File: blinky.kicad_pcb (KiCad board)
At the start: 2 copper layers, 69.9 x 70 mm, 58 parts, among them J1 MIC_CLK, J10 DEBUG, J11 SWD, J12 BATTERY, J13 UART, J14 5V, J15 3V3, J2 MIC_DOUT, J3 LED_DIN, J4 ACCEL_MISO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

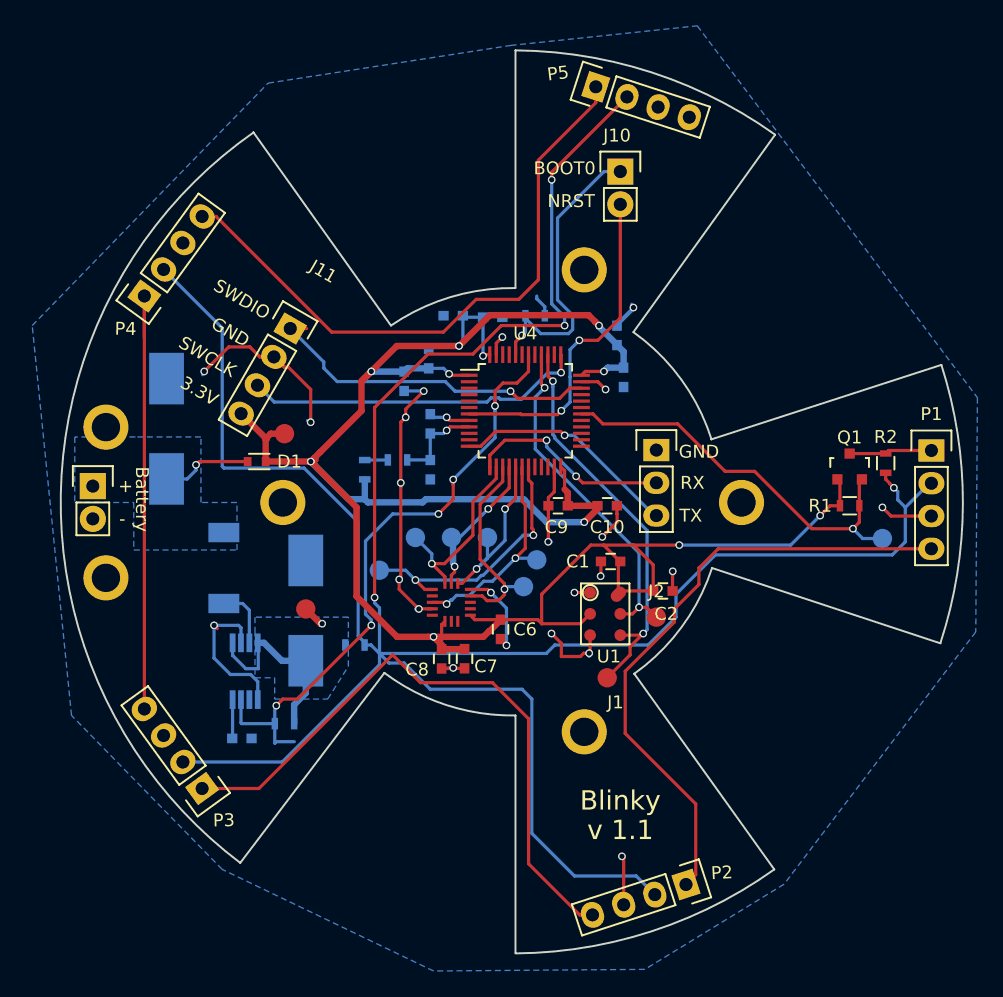
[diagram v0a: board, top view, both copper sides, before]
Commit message: Add heartbeat led
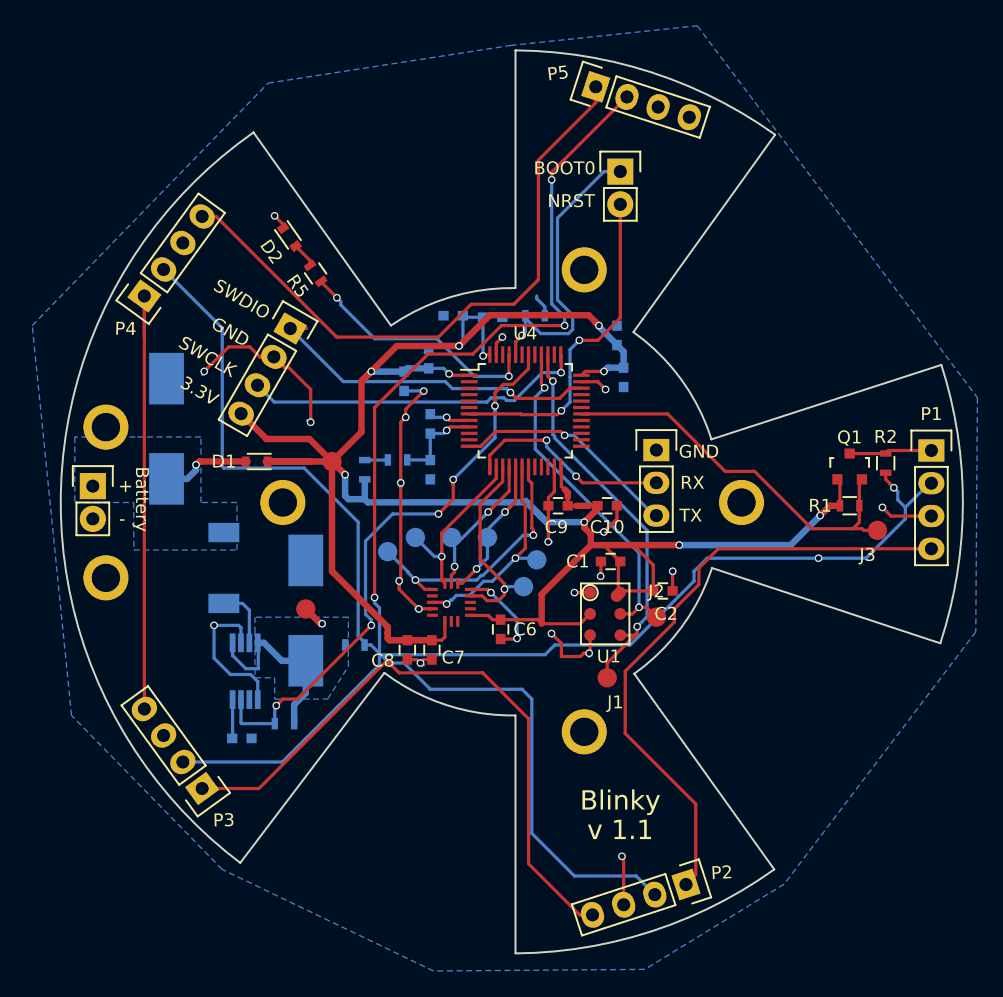
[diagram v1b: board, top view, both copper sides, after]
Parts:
- added D2: LED, Diodes_SMD:D_0603, F.Cu at (114.8, 53.1)
- added R5: 0, Resistors_SMD:R_0603, F.Cu at (116.8, 55.9)
- D1: value D_Schottky_0.5A_20V -> D_Schottky_0.1A_30V; footprint Diodes_SMD:SOD-523 -> Diodes_SMD:D_0603
- J3: moved to F.Cu
- moved J15 4.27 mm to (118.1, 70.5)
- moved C8 2.75 mm to (124.0, 85.1)
- moved C7 2.62 mm to (125.9, 85.1)
- moved J9 1.58 mm to (122.4, 77.5)
- moved J3 0.74 mm to (160.4, 75.8)
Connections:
- U4 pad 45: /MCU/PB8 -> /LED_HB
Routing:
- net /LED_HB: track 0.00 -> 19.5 mm, vias 0 -> 2
- net /POWER_LBO: track 48.5 -> 45.2 mm
- net GND: track 95.8 -> 92.9 mm
- net Net-(D2-Pad2): track 0.00 -> 1.97 mm
- net /ACCEL_MISO: track 13.2 -> 11.5 mm
- net Net-(P1-Pad2): track 206.9 -> 205.3 mm, vias 4 -> 5
- net /ACCEL_CS: track 14.7 -> 13.5 mm
- net +3V3: track 182.6 -> 181.9 mm, vias 11 -> 10
- net /LED_DATAIN: track 31.4 -> 30.8 mm, vias 1 -> 0
- net /MIC_CLK: track 31.3 -> 30.8 mm
- net Net-(P2-Pad4): track 49.5 -> 49.0 mm

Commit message: Add shortcut to enable 3V3 Only mode
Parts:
- added R8: 0, Resistors_SMD:R_0805, F.Cu at (118.1, 81.0)
- moved J14 3.42 mm to (112.8, 81.0)
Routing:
- net GND: track 92.9 -> 116.5 mm, vias 24 -> 28
- net +5V: track 18.3 -> 20.4 mm, vias 1 -> 2
- net +3V3: track 181.9 -> 180.7 mm

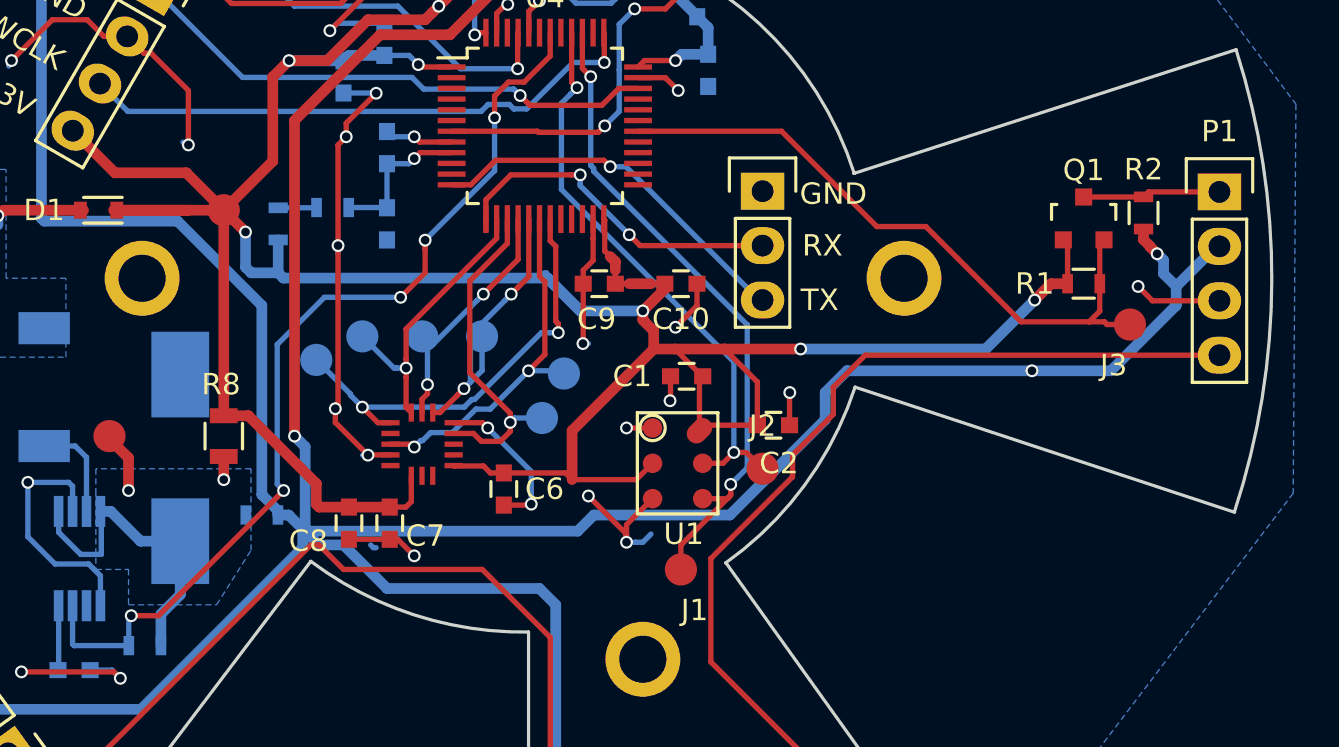
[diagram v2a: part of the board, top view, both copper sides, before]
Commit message: change level shifter
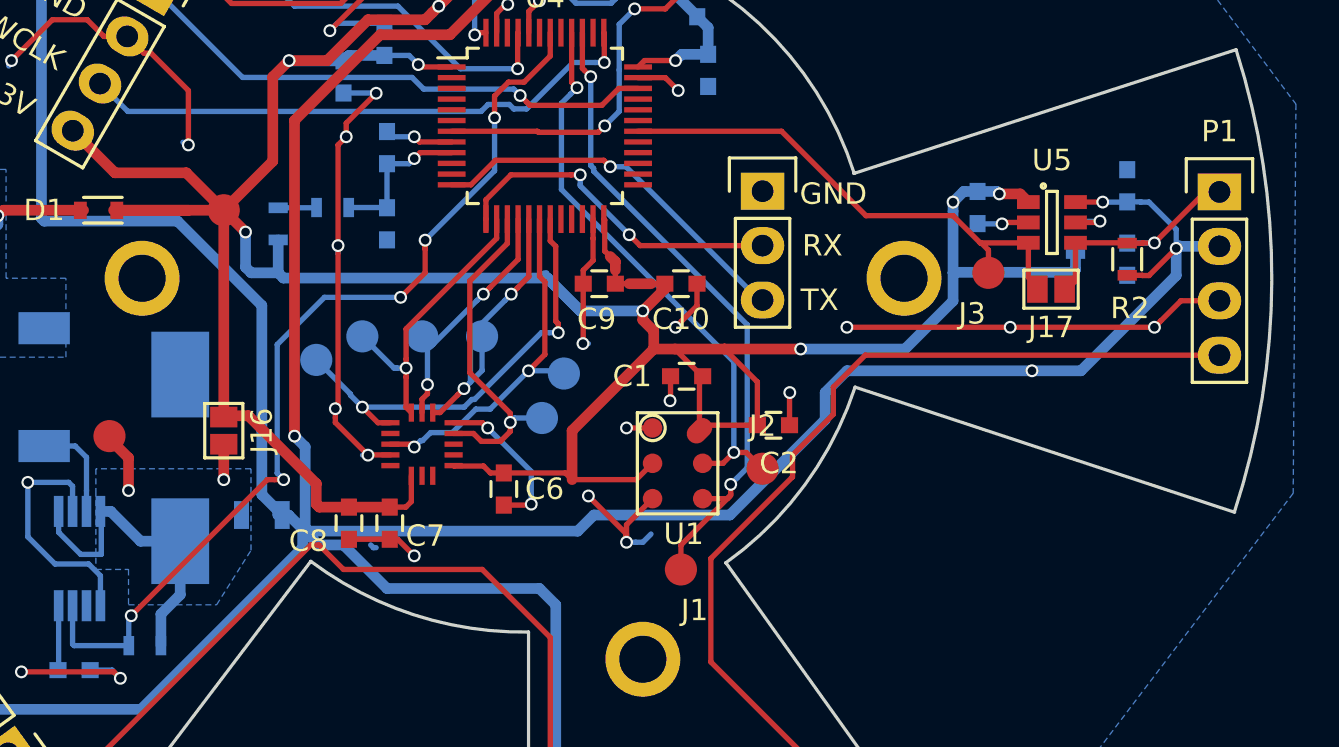
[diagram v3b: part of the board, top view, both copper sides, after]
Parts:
- removed Q1: BSS138, TO_SOT_Packages_SMD:SOT-23
- removed R8: 0, Resistors_SMD:R_0805
- added C19: 100nF, Capacitors_SMD:C_0603, B.Cu at (153.3, 70.4)
- added C20: NA, Capacitors_SMD:C_0603, B.Cu at (160.3, 69.3)
- added C21: NA, Capacitors_SMD:C_0603, B.Cu at (160.3, 72.8)
- added J16: GS2, Connectors:GS2, F.Cu at (118.1, 80.8)
- added J17: GS2, Connectors:GS2, F.Cu at (156.7, 74.2)
- added U5: TXS0101, TO_SOT_Packages_SMD:SOT-23-6, F.Cu at (156.8, 71.1)
- R1: value 10k -> NA; moved to B.Cu
- R2: value 10k -> NA
- R4: footprint Resistors_SMD:R_0603 -> Resistors_SMD:R_0805
- moved J3 7.03 mm to (153.8, 73.4)
- moved R2 2.29 mm to (160.3, 72.8)
- moved R1 2.19 mm to (157.9, 71.8), turned to 90 degrees
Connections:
- net Net-(P1-Pad1) renamed /LED5V_DATAIN
- net Net-(P1-Pad2) renamed /LED_5V
- R1 pad 2: /LED_DATAIN -> Net-(R1-Pad2)
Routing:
- net GND: track 116.5 -> 132.7 mm, vias 28 -> 31
- net +3V3: track 180.7 -> 188.0 mm, vias 10 -> 11
- net /LED_DATAIN: track 30.8 -> 24.3 mm
- net /LED_5V: track 205.3 -> 211.1 mm, vias 5 -> 6
- net /LED5V_DATAIN: track 6.44 -> 11.3 mm, vias 0 -> 1
- net Net-(R1-Pad2): track 0.00 -> 2.32 mm, vias 0 -> 1
- net +5V: track 20.4 -> 21.0 mm

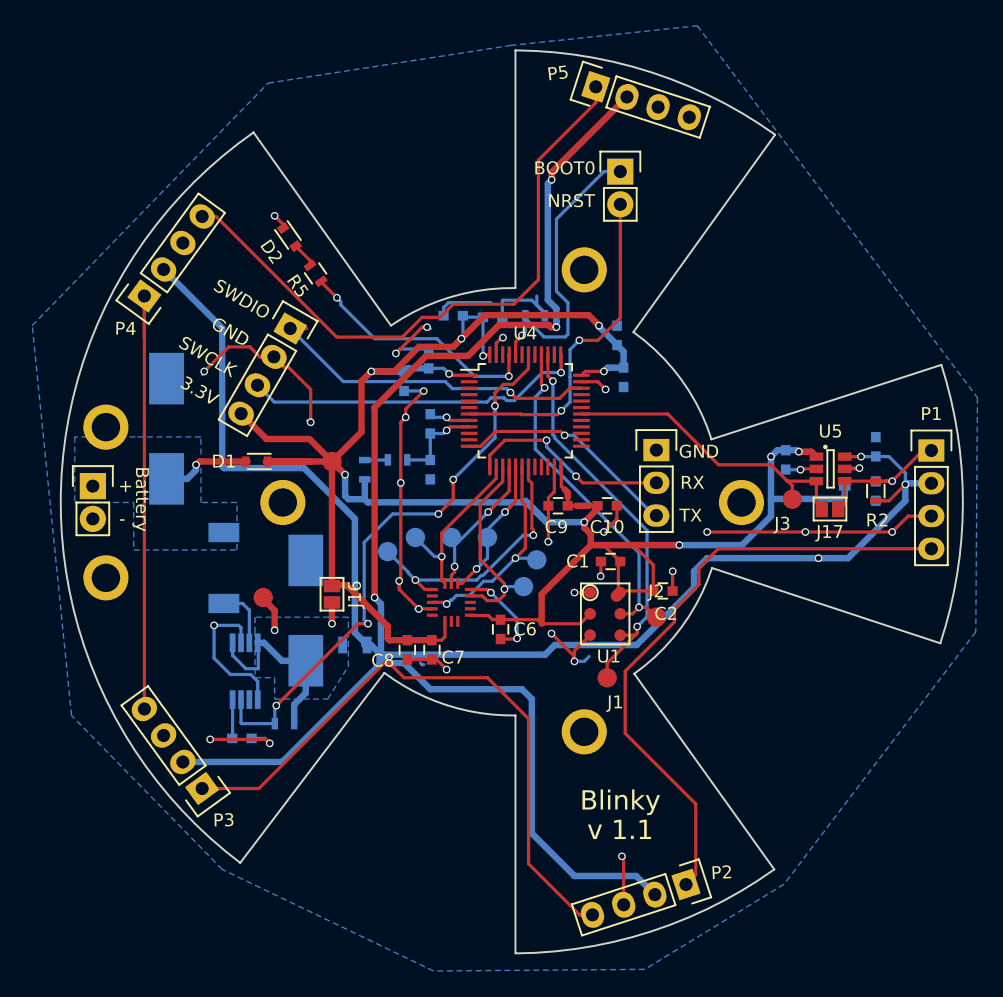
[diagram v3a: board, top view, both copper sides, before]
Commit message: uses 2mm pitch pin header for neopixel
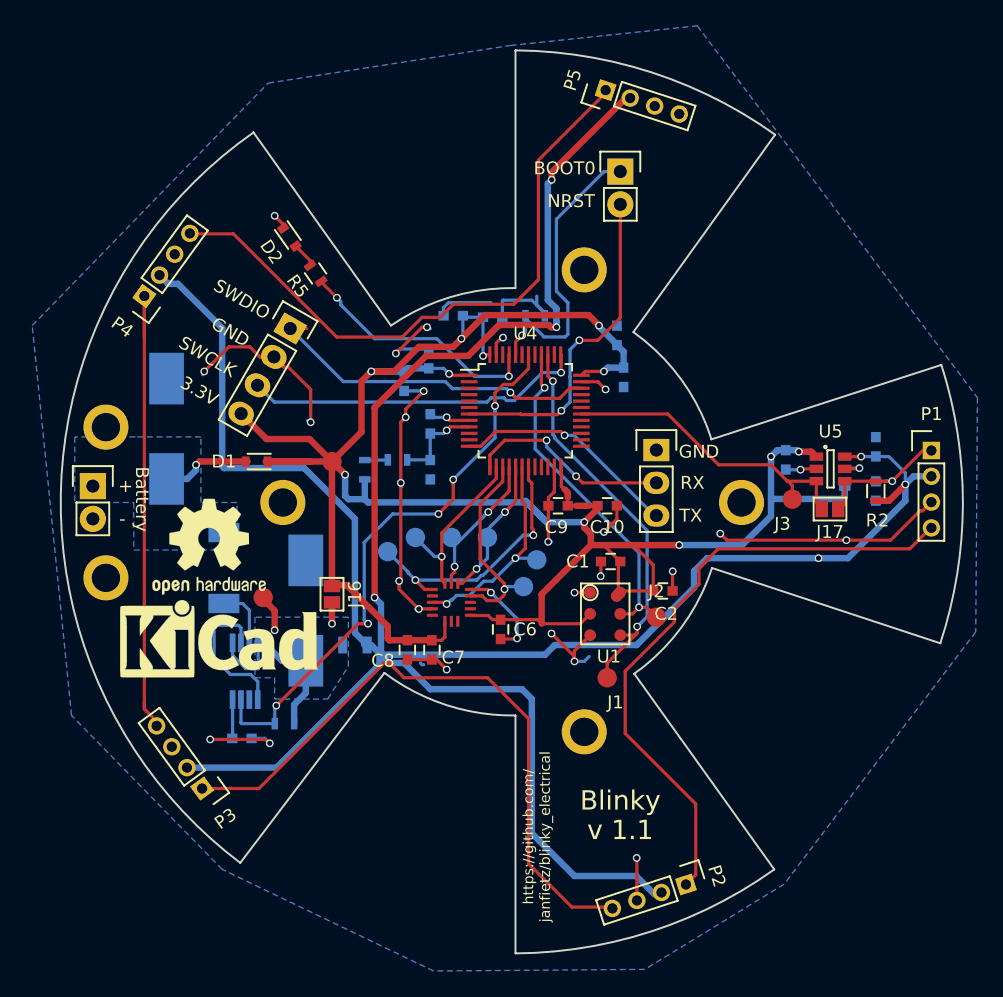
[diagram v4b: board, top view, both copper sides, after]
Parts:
- added REF***: KiCad-Logo_6mm_SilkScreen, Symbols:KiCad-Logo_6mm_SilkScreen, F.Cu at (109.3, 84.2)
- added REF***: OSHW-Logo2_9.8x8mm_SilkScreen, Symbols:OSHW-Logo2_9.8x8mm_SilkScreen, F.Cu at (108.6, 77.1)
- P1, P2, P3, P4, P5: footprint Pin_Headers:Pin_Header_Straight_1x04 -> Pin_Headers:Pin_Header_Straight_1x04_Pitch2.00mm
- moved P5 0.80 mm to (139.3, 41.7)
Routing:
- net Net-(P3-Pad4): track 36.7 -> 38.4 mm
- net Net-(P2-Pad4): track 49.0 -> 50.2 mm
- net Net-(P1-Pad4): track 48.1 -> 48.8 mm
- net /LED_5V: track 211.1 -> 211.8 mm
- net GND: track 132.7 -> 132.1 mm, vias 31 -> 30
- net Net-(P4-Pad4): track 48.6 -> 49.1 mm
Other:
- board text added: "https://github.com/ janfietz/blinky_electrical"

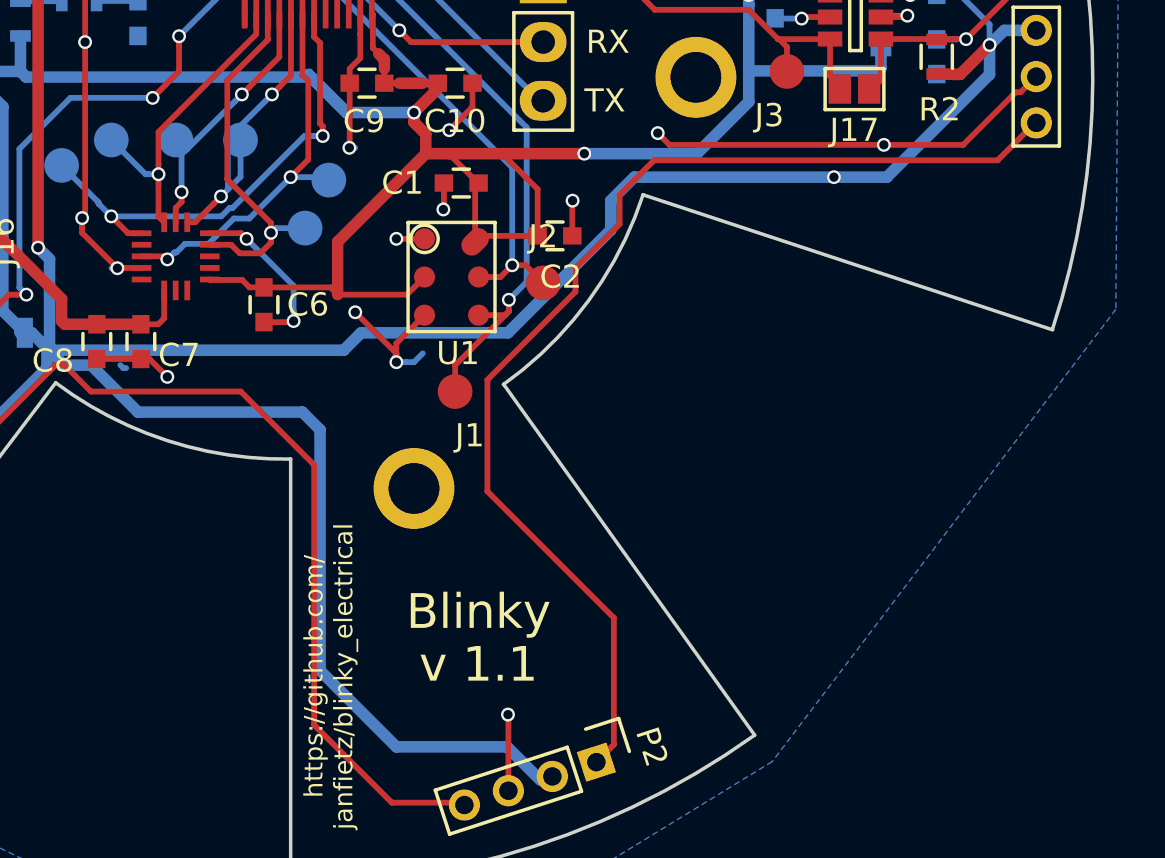
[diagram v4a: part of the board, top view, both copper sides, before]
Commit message: pcb: add qr code and axis
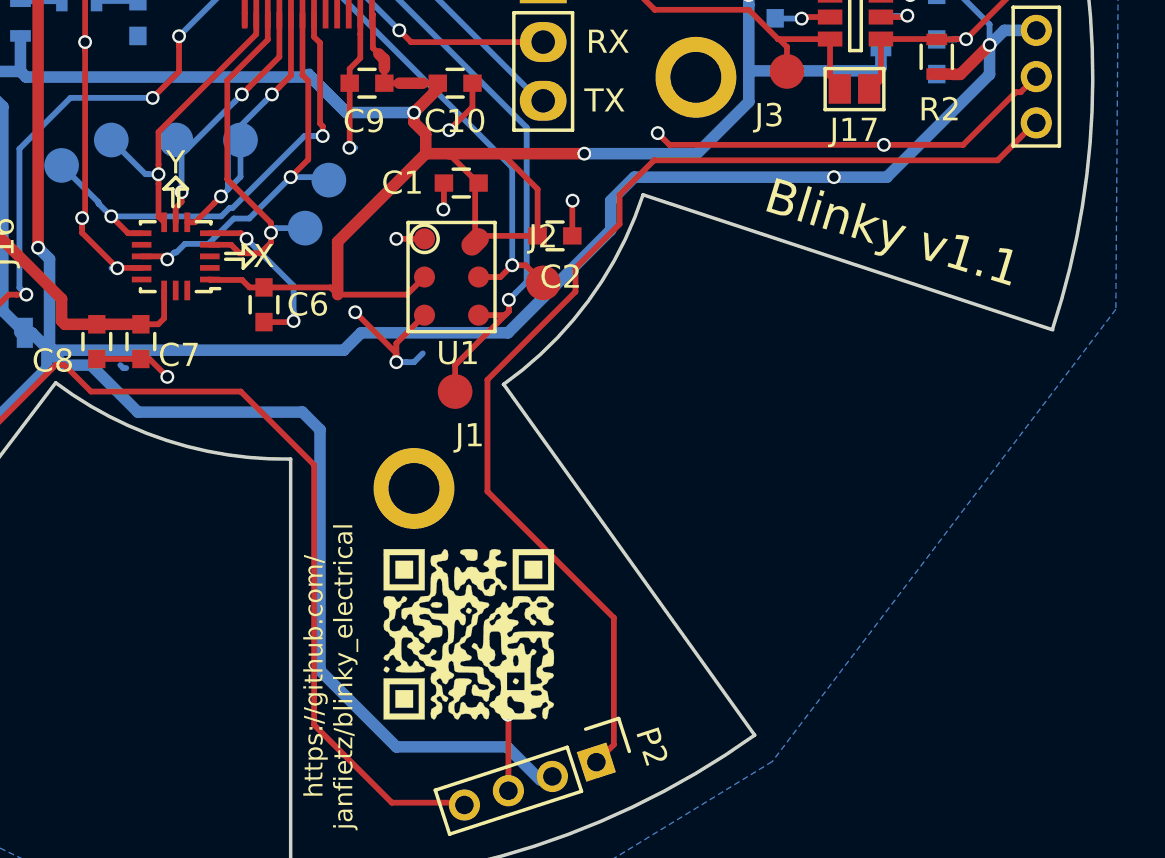
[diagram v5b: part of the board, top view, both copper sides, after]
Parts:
- added G***: LOGO, jfilogos:qrblinky_8x8, F.Cu at (140.1, 97.8)
- U3: footprint tinkerforge:LGA-16-3x3 -> LGA-16-3x3_Axis
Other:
- board text added: "Blinky v1.1"
- board text removed: "Blinky"
- board text removed: "v 1.1"
